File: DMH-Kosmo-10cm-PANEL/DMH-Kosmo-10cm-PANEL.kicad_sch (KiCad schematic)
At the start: 4 parts

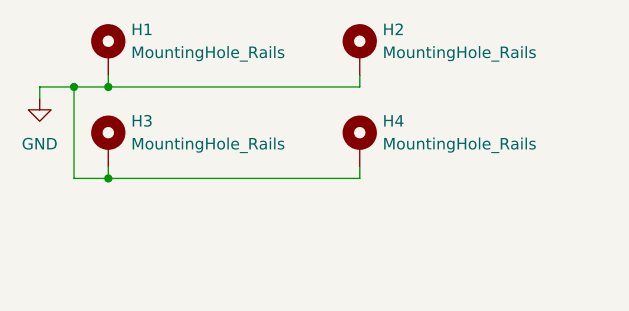
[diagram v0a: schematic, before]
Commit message: Updated 5cm and 10 templates
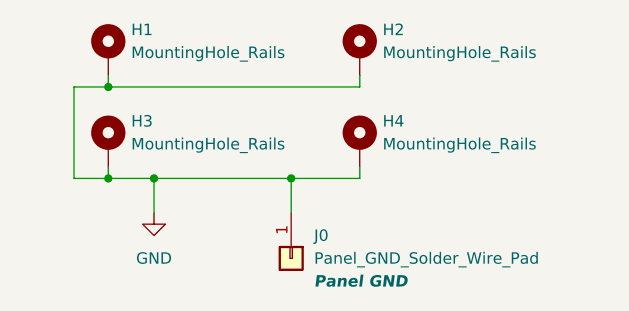
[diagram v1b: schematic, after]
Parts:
- added J0: Panel_GND_Solder_Wire_Pad, SynthStuff:Panel_GND_SolderWirePad_5x10mm, symbol SynthStuff:Panel_GND_Solder_Wire_Pad
- H1, H2, H3, H4: footprint SynthStuff:MountingHole_Slotted_Rails -> SynthStuff:MountingHole_Rails
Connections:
- net GND: now also J0.1 (Pin_1)
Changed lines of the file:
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@@
+	)
+	(junction
+		(at 33.02 269.24)
+		(diameter 0)
+		(color 0 0 0 0)
+	)
+	(junction
+		(at 48.26 269.24)
+		(diameter 0)
+		(color 0 0 0 0)
 	)
 	(junction
@@
 		(color 0 0 0 0)
 	)
-	(junction
-		(at 24.13 259.08)
-		(diameter 0)
-		(color 0 0 0 0)
-	)
-	(wire
-		(pts
-			(xy 55.88 259.08) (xy 27.94 259.08)
-		)
-		(stroke
-			(width 0)
-			(type default)
-		)
-	)
 	(wire
 		(pts
@@
 	(wire
 		(pts
-			(xy 20.32 259.08) (xy 24.13 259.08)
+			(xy 27.94 259.08) (xy 55.88 259.08)
 		)
 		(stroke
@@
 	(wire
 		(pts
-			(xy 20.32 260.35) (xy 20.32 259.08)
+			(xy 48.26 269.24) (xy 48.26 273.05)
 		)
 		(stroke
@@
 	(wire
 		(pts
+			(xy 33.02 269.24) (xy 33.02 273.05)
+		)
+		(stroke
+			(width 0)
+			(type default)
+		)
+	)
+	(wire
+		(pts
 			(xy 24.13 259.08) (xy 24.13 269.24)
 		)
@@
 	(wire
 		(pts
-			(xy 55.88 269.24) (xy 27.94 269.24)
+			(xy 48.26 269.24) (xy 55.88 269.24)
+		)
+		(stroke
+			(width 0)
+			(type default)
+		)
+	)
+	(wire
+		(pts
+			(xy 27.94 269.24) (xy 33.02 269.24)
+		)
+		(stroke
+			(width 0)
+			(type default)
+		)
+	)
+	(wire
+		(pts
+			(xy 33.02 269.24) (xy 48.26 269.24)
 		)
 		(stroke
@@
 			)
 		)
-		(property "Footprint" "SynthStuff:MountingHole_Slotted_Rails"
+		(property "Footprint" "SynthStuff:MountingHole_Rails"
 			(at 55.88 255.27 0)
 			(effects
@@
 	(symbol
 		(lib_id "power:GND")
-		(at 20.32 260.35 0)
+		(at 33.02 273.05 0)
 		(unit 1)
 		(exclude_from_sim no)
@@
 		(fields_autoplaced yes)
 		(property "Reference" "#PWR01"
-			(at 20.32 266.7 0)
+			(at 33.02 279.4 0)
 			(effects
 				(font
@@
 		)
 		(property "Value" "GND"
-			(at 20.32 265.43 0)
+			(at 33.02 278.13 0)
 			(effects
 				(font
@@
 		)
 		(property "Footprint" ""
-			(at 20.32 260.35 0)
+			(at 33.02 273.05 0)
 			(effects
 				(font
@@
 		)
 		(property "Datasheet" ""
-			(at 20.32 260.35 0)
+			(at 33.02 273.05 0)
 			(effects
 				(font
@@
 		)
 		(property "Description" "Power symbol creates a global label with name \"GND\" , ground"
-			(at 20.32 260.35 0)
+			(at 33.02 273.05 0)
 			(effects
 				(font
@@
 			)
 		)
-		(property "Footprint" "SynthStuff:MountingHole_Slotted_Rails"
+		(property "Footprint" "SynthStuff:MountingHole_Rails"
 			(at 27.94 265.43 0)
 			(effects
@@
 			)
 		)
-		(property "Footprint" "SynthStuff:MountingHole_Slotted_Rails"
+		(property "Footprint" "SynthStuff:MountingHole_Rails"
 			(at 55.88 265.43 0)
 			(effects
@@
 				(path "/a552705f-a9fe-462e-9913-5cfcc08b233c"
 					(reference "H4")
+					(unit 1)
+				)
+			)
+		)
+	)
+	(symbol
+		(lib_id "SynthStuff:Panel_GND_Solder_Wire_Pad")
+		(at 48.26 278.13 270)
+		(unit 1)
+		(exclude_from_sim no)
+		(in_bom no)
+		(on_board yes)
+		(dnp no)
+		(fields_autoplaced yes)
+		(property "Reference" "J0"
+			(at 50.8 275.5899 90)
+			(effects
+				(font
+					(size 1.27 1.27)
+				)
+				(justify left)
+			)
+		)
+		(property "Value" "Panel_GND_Solder_Wire_Pad"
+			(at 50.8 278.1299 90)
+			(effects
+				(font
+					(size 1.27 1.27)
+				)
+				(justify left)
+			)
+		)
+		(property "Footprint" "SynthStuff:Panel_GND_SolderWirePad_5x10mm"
+			(at 48.26 278.13 0)
+			(effects
+				(font
+					(size 1.27 1.27)
+				)
+				(hide yes)
+			)
+		)
+		(property "Datasheet" "~"
+			(at 48.26 278.13 0)
+			(effects
+				(font
+					(size 1.27 1.27)
+				)
+				(hide yes)
+			)
+		)
+		(property "Description" "Solder pad to allow connection between PCB and Front Panel"
+			(at 48.26 278.13 0)
+			(effects
+				(font
+					(size 1.27 1.27)
+				)
+				(hide yes)
+			)
+		)
+		(property "Function" "Panel GND"
+			(at 50.8 280.67 90)
+			(effects
+				(font
+					(size 1.27 1.27)
+					(thickness 0.254)
+					(bold yes)
+					(italic yes)
+				)
+				(justify left)
+			)
+		)
+		(pin "1"
+		)
+		(instances
+			(project ""
+				(path "/a552705f-a9fe-462e-9913-5cfcc08b233c"
+					(reference "J0")
 					(unit 1)
 				)
@@
 			)
 		)
-		(property "Footprint" "SynthStuff:MountingHole_Slotted_Rails"
+		(property "Footprint" "SynthStuff:MountingHole_Rails"
 			(at 27.94 255.27 0)
 			(effects
@@
 			)
 		)
+		(property "Function" ""
+			(at 27.94 255.27 0)
+			(effects
+				(font
+					(size 1.27 1.27)
+				)
+			)
+		)

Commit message: Changed panel GND pad function to just GND
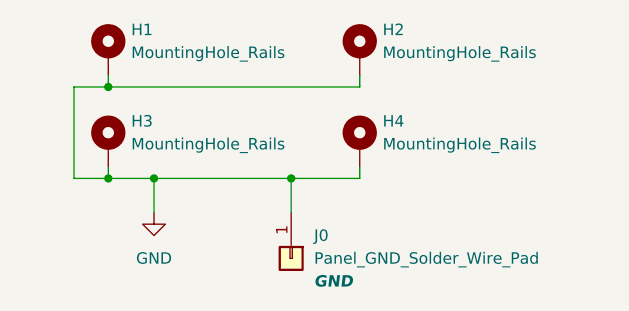
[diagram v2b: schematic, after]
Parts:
- J0: Function Panel GND -> GND
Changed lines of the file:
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@@
 			)
 		)
-		(property "Function" "Panel GND"
+		(property "Function" "GND"
 			(at 50.8 280.67 90)
 			(effects

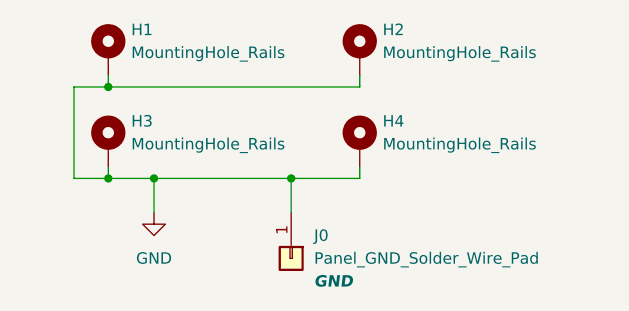
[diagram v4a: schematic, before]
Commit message: Matched main PCB size reference in PANEL templates
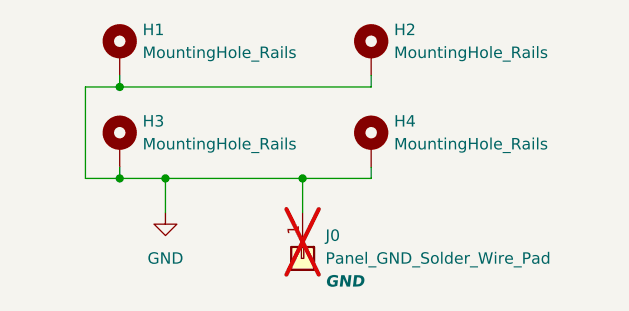
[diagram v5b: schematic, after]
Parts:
- J0: now not fitted
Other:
- moved on the sheet: H1, H2, H3, H4
